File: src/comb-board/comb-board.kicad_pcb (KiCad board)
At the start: 2 copper layers, 114.5 x 10.4 mm, 11 parts, among them J1 Game_Connector, Q1 BC337, Q2 BC327, U1 ATmega328-PU, Y1 16MHz

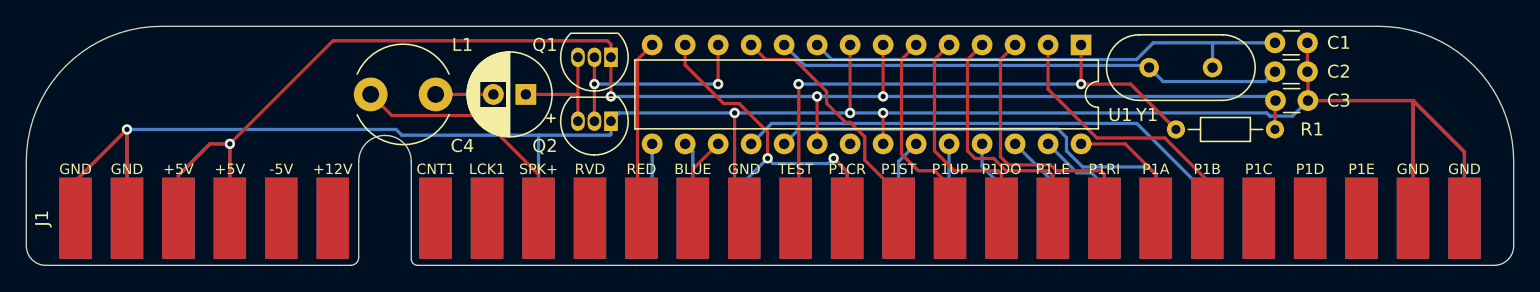
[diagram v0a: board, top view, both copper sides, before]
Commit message: Fix DRC.
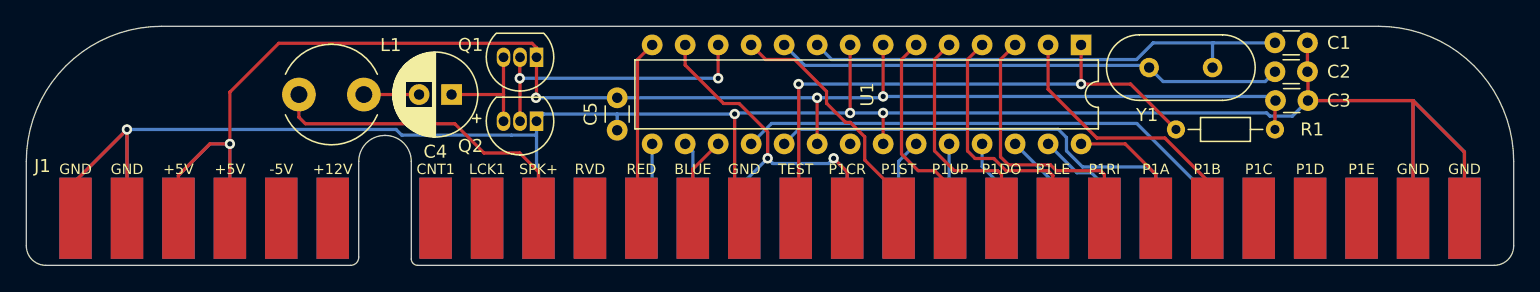
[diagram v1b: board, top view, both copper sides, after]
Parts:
- added C5: 100nF, Capacitor_THT:C_Disc_D3.0mm_W1.6mm_P2.50mm, F.Cu at (140.5, 103.2)
- C4: value CP -> 47u
- U1: value ATmega328-PU -> ATmega328P-P
- moved Q1 5.73 mm to (134.3, 97.6)
- moved Q2 5.73 mm to (134.3, 102.6)
- moved C4 5.72 mm to (127.8, 100.5)
- moved L1 5.52 mm to (121.0, 100.5)
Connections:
- J1 pad 11: Net-(J1-Pad11) -> unconnected-(J1-Pad11)
- J1 pad 24: Net-(J1-Pad24) -> unconnected-(J1-Pad24)
- J1 pad 25: Net-(J1-Pad25) -> unconnected-(J1-Pad25)
- J1 pad 26: Net-(J1-Pad26) -> unconnected-(J1-Pad26)
- J1 pad 5: Net-(J1-Pad5) -> unconnected-(J1-Pad5)
- J1 pad 6: Net-(J1-Pad6) -> unconnected-(J1-Pad6)
- J1 pad 8: Net-(J1-Pad8) -> unconnected-(J1-Pad8)
- J1 pad 9: Net-(J1-Pad9) -> unconnected-(J1-Pad9)
- J1 pad AB: Net-(J1-PadAB) -> unconnected-(J1-PadAB)
- J1 pad AC: Net-(J1-PadAC) -> unconnected-(J1-PadAC)
- J1 pad AD: Net-(J1-PadAD) -> unconnected-(J1-PadAD)
- J1 pad E: Net-(J1-PadE) -> unconnected-(J1-PadE)
- J1 pad F: Net-(J1-PadF) -> unconnected-(J1-PadF)
- J1 pad J: Net-(J1-PadJ) -> unconnected-(J1-PadJ)
- J1 pad K: Net-(J1-PadK) -> unconnected-(J1-PadK)
- J1 pad M: Net-(J1-PadM) -> unconnected-(J1-PadM)
- J1 pad S: Net-(J1-PadS) -> unconnected-(J1-PadS)
- U1 pad 21: Net-(U1-Pad21) -> unconnected-(U1-Pad21)
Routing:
- net SPEAKER+: track 18.8 -> 25.5 mm
- net SPEAKER_PWM: track 17.5 -> 22.8 mm
- net +5V: track 125.9 -> 128.0 mm
- net GND: track 206.2 -> 207.5 mm
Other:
- net class Default removed
